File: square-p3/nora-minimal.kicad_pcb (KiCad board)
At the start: 2 copper layers, 49.5 x 49.5 mm, 15 parts, among them J1 UP2-AH-1-TH, J2 SWD / 3V3, J3 GPIO / 3V3, U1 NORA-B106-00B, U2 XC6206P332MR-G, U3 USBLC6-2SC6

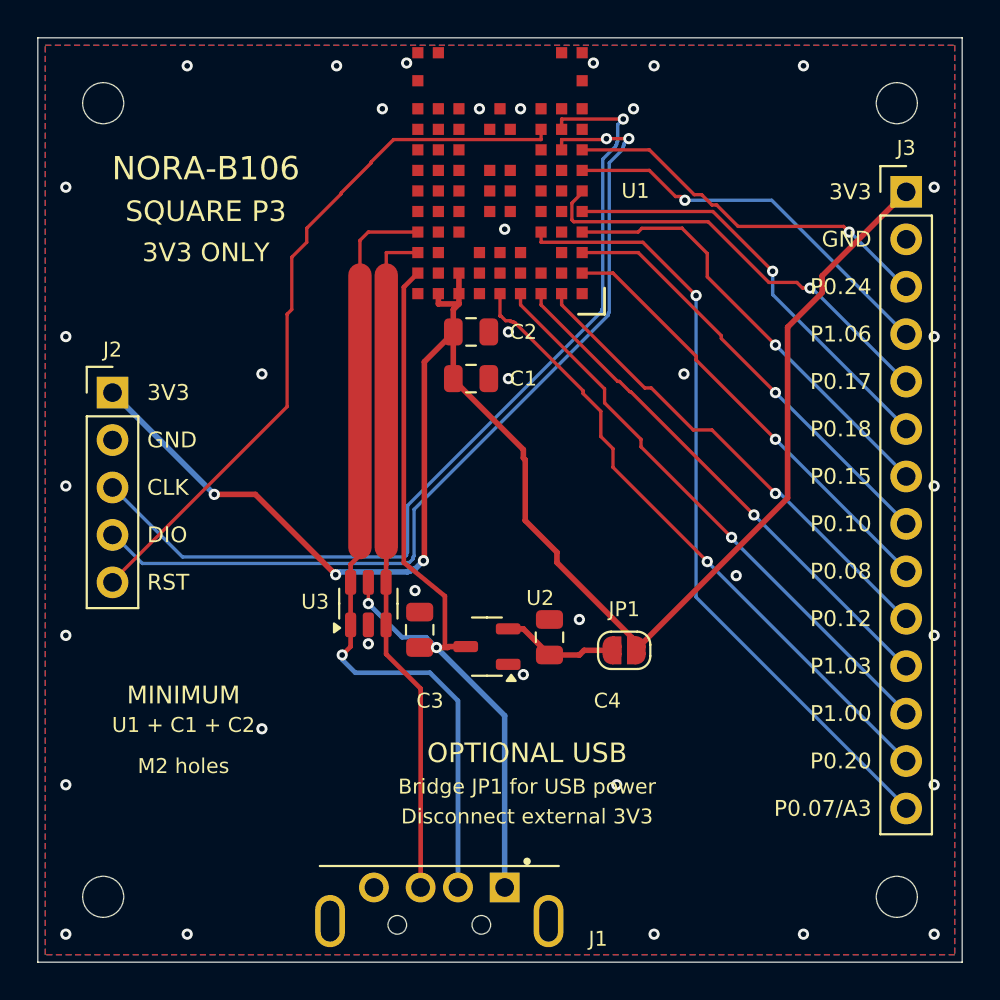
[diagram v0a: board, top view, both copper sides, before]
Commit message: Narrow P3 board, centre USB and add cyber dragon artwork and optional reset
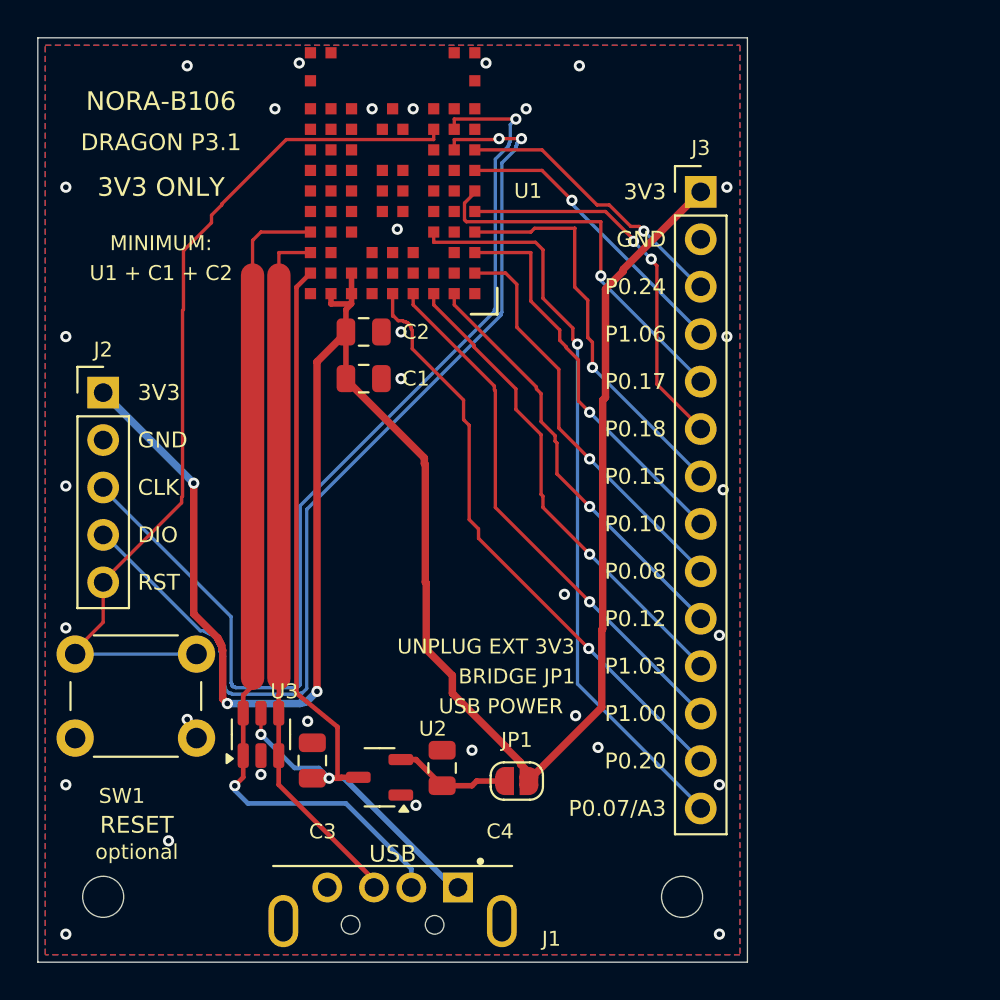
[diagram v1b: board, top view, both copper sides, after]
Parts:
- removed the H1 at (3.50, 3.50)
- removed the H2 at (46.0, 3.50)
- added SW1: RESET (optional), Breakout:SW_PUSH_6mm, F.Cu at (2.00, 33.0)
- moved H2 11.5 mm to (34.5, 46.0)
- moved J3 11.0 mm to (35.5, 8.25)
- moved C3 9.06 mm to (14.7, 38.7)
- moved C4 9.06 mm to (21.6, 39.1)
- moved JP1 9.06 mm to (25.6, 39.8)
- moved U2 9.06 mm to (18.3, 39.6)
- moved U3 9.06 mm to (11.9, 37.3)
- moved C1 5.75 mm to (17.4, 18.2)
- moved C2 5.75 mm to (17.4, 15.8)
- moved U1 5.75 mm to (19.0, 8.20)
- moved J1 2.50 mm to (19.0, 45.5)
- moved J2 0.50 mm to (3.50, 19.0)
- renumbered H3 to H1, H4 to H2
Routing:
- net /+3V3: track 90.5 -> 112.8 mm
- net /RESET_N: track 38.4 -> 47.2 mm
- net /SWCLK: track 49.3 -> 56.2 mm
- net /SWDIO: track 48.3 -> 54.3 mm
- net /P0.24: track 20.4 -> 15.1 mm
- net /P1.06: track 21.0 -> 15.9 mm
- net /P0.17: track 23.3 -> 19.8 mm
- net /P0.12: track 26.0 -> 22.9 mm
- net /P1.03: track 28.2 -> 25.9 mm
- net /P0.10: track 23.5 -> 21.3 mm
- net /P0.18: track 22.9 -> 20.8 mm, vias 1 -> 2
- net /P1.00: track 31.0 -> 28.9 mm
- net /P0.20: track 34.3 -> 32.1 mm
- net /P0.15: track 23.7 -> 21.5 mm
- net /P0.08: track 24.1 -> 21.9 mm
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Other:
- board size 49.5 x 49.5 mm -> 38 x 49.5 mm
- board text added: "38 x 49.5 mm"
- board text added: "BRIDGE JP1"
- board text added: "Codex + Backplane"
- board text added: "DRAGON P3.1"
- board text added: "MINIMUM:"
- board text added: "NORA DRAGON P3.1"
- board text added: "RESET"
- board text added: "UNPLUG EXT 3V3"
- board text added: "USB"
- board text added: "USB POWER"
- board text added: "optional"
- board text removed: "49.5 x 49.5 mm"
- board text removed: "Bridge JP1 for USB power"
- board text removed: "Codex"
- board text removed: "Designed by"
- board text removed: "Disconnect external 3V3"
- board text removed: "JP1 = USB POWER"
- board text removed: "M2 holes"
- board text removed: "MINIMUM"
- board text removed: "NORA SQUARE P3"
- board text removed: "OPTIONAL USB"
- board text removed: "SQUARE P3"
- board text removed: "with Backplane"

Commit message: Switch Dragon P3.2 to USB-C and restore four mounting holes
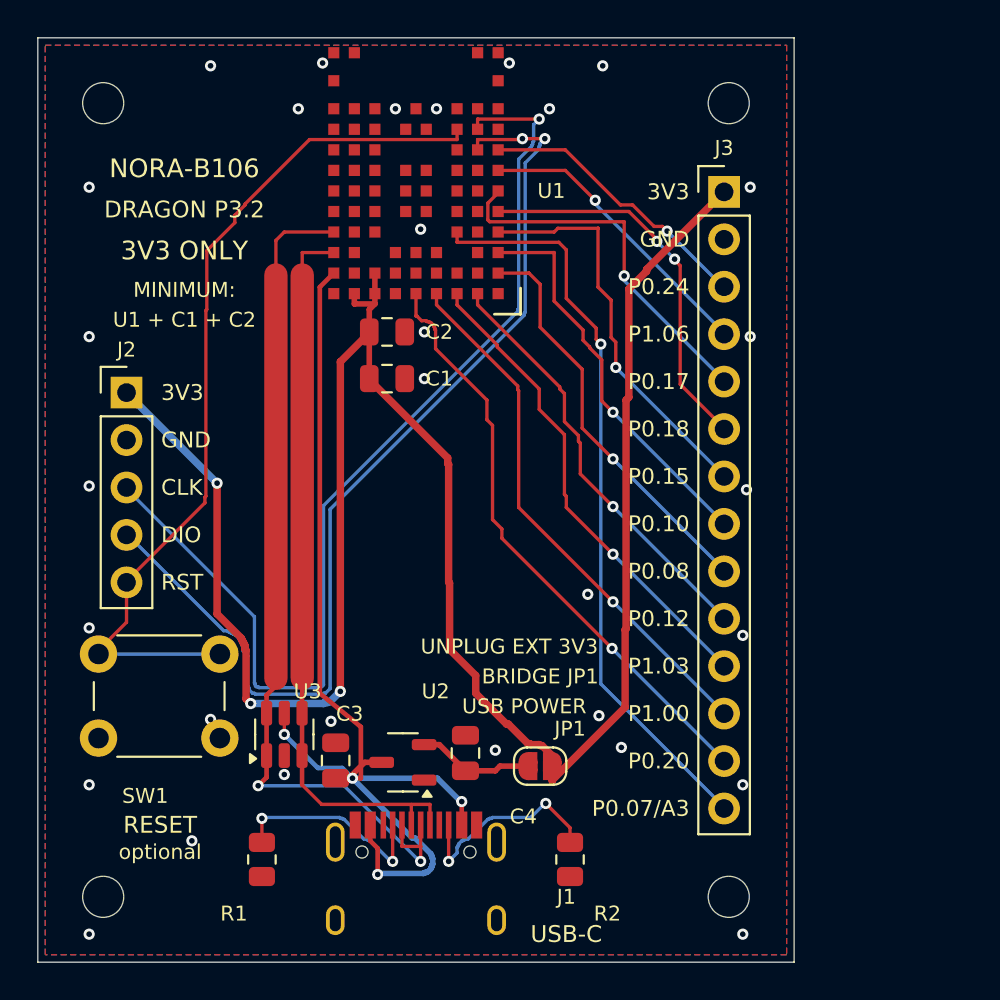
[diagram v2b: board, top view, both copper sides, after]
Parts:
- added H3: MountingHole_2.2mm_M2, Breakout:MountingHole_2.2mm_M2, F.Cu at (3.50, 3.50)
- added H4: MountingHole_2.2mm_M2, Breakout:MountingHole_2.2mm_M2, F.Cu at (37.0, 3.50)
- added R1: 5k1/1%, Breakout:R_0805_2012Metric, F.Cu at (12.0, 44.0)
- added R2: 5k1/1%, Breakout:R_0805_2012Metric, F.Cu at (28.5, 44.0)
- J1: value UP2-AH-1-TH -> TYPE-C-31-M-12; footprint Breakout:USB_A_UP2-AH-1-TH -> Breakout:USB_C_Receptacle_HRO_TYPE-C-31-M-12
- moved H2 2.50 mm to (37.0, 46.0)
- moved C4 1.48 mm to (22.9, 38.3)
- moved U2 1.48 mm to (19.6, 38.8)
- moved JP1 1.48 mm to (26.9, 39.0)
- moved J1 1.43 mm to (20.2, 46.2)
- moved C1 1.25 mm to (18.7, 18.2)
- moved C2 1.25 mm to (18.7, 15.8)
- moved C3 1.25 mm to (15.9, 38.7)
- moved J2 1.25 mm to (4.75, 19.0)
- moved J3 1.25 mm to (36.8, 8.25)
- moved SW1 1.25 mm to (3.25, 33.0)
- moved U1 1.25 mm to (20.2, 8.20)
- moved U3 1.25 mm to (13.2, 37.3)
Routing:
- net /VBUS: track 47.3 -> 59.4 mm, vias 2 -> 4
- net /CC2: track 0.00 -> 11.3 mm, vias 0 -> 2
- net /CC1: track 0.00 -> 11.2 mm, vias 0 -> 2
- net /USB_DM: track 45.3 -> 47.3 mm, vias 1 -> 2
- net /USB_DP: track 37.8 -> 39.7 mm
- net /GND: vias 32 -> 31
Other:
- board size 38 x 49.5 mm -> 40.5 x 49.5 mm
- board text added: "40.5 x 49.5 mm"
- board text added: "DRAGON P3.2"
- board text added: "NORA DRAGON P3.2"
- board text added: "USB-C"
- board text removed: "38 x 49.5 mm"
- board text removed: "DRAGON P3.1"
- board text removed: "NORA DRAGON P3.1"
- board text removed: "USB"

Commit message: Update JLCPCB order settings and remove retired order-number marker
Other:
- board text removed: "JLCJLCJLCJLC"
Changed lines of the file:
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@@
-		)
-	)
-	(gr_text "JLCJLCJLCJLC"
-		(at 31.25 47.8 0)
-		(layer "B.SilkS")
-		(effects
-			(font
-				(size 0.8 0.8)
-				(thickness 0.15)
-			)
-			(justify mirror)
 		)
 	)

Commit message: Remove owner references and back title and dimensions from PCB
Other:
- board text removed: "40.5 x 49.5 mm"
- board text removed: "NORA DRAGON P3.2"
- board text removed: "for rain-1"
- board text removed: "github.com/rain-1/nora-b106"
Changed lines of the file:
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@@
-		)
-	)
-	(gr_text "40.5 x 49.5 mm"
-		(at 20.25 8.7 0)
-		(layer "B.SilkS")
-		(effects
-			(font
-				(size 0.9 0.9)
-				(thickness 0.15)
-			)
-			(justify mirror)
-		)
-	)
-	(gr_text "github.com/rain-1/nora-b106"
-		(at 20.25 11.8 0)
-		(layer "B.SilkS")
-		(effects
-			(font
-				(size 0.8 0.8)
-				(thickness 0.15)
-			)
-			(justify mirror)
-		)
-	)
-	(gr_text "NORA DRAGON P3.2"
-		(at 20.25 6.7 0)
-		(layer "B.SilkS")
-		(effects
-			(font
-				(size 1 1)
-				(thickness 0.15)
-			)
-			(justify mirror)
 		)
 	)
@@
 				(thickness 0.15)
 			)
-			(justify mirror)
-		)
-	)
-	(gr_text "for rain-1"
-		(at 20.25 40.4 0)
-		(layer "B.SilkS")
-		(effects
-			(font
-				(size 0.9 0.9)
-				(thickness 0.15)
-			)

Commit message: Remove prototype label from back silkscreen
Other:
- board text removed: "PROTO / UNTESTED"
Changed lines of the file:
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@@
-		)
-	)
-	(gr_text "PROTO / UNTESTED"
-		(at 20.25 10.7 0)
-		(layer "B.SilkS")
-		(effects
-			(font
-				(size 0.8 0.8)
-				(thickness 0.15)
-			)
-			(justify mirror)
 		)
 	)
